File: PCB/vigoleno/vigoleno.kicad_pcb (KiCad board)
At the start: 6 copper layers, 80.8 x 50 mm, 181 parts, among them J1 9P-MSD-PP-V2, J3 USB_OTG, J4 IPEX RF Coaxial Connector SMD, M1 MODULE_RTL8188, U1 MT29F8G08ABABA, U2 ISL8022, U3 ALLWINNER-A13(176-LQFP), U4 TLV62569-SOT23-6, U5 TPS62233DRYR, U6 AS4C256M16D3A-12BAN(96-FBGA), U7 MCP130T-300ITT, Y1 Crystal_GND24_24MHz

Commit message: update March 6 2019
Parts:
- C31, C32, Y1: moved to B.Cu
- moved DEBUG1 49.6 mm to (589.9, -415.9), turned to 180 degrees
- moved D3 24.8 mm to (582.5, -418.7), turned to 0 degrees
- moved J4 24.7 mm to (556.2, -446.9)
- moved D2 19.0 mm to (582.5, -421.9), turned to 0 degrees
- moved JP2 15.2 mm to (558.4, -457.5), turned to 270 degrees
- moved C97 12.6 mm to (560.9, -456.8), turned to 180 degrees
- moved L6 11.8 mm to (558.4, -454.4), turned to 270 degrees
- moved C98 10.7 mm to (561.4, -455.6), turned to 180 degrees
- moved C31 10.5 mm to (613.0, -432.0), turned to 0 degrees
- moved C32 7.32 mm to (615.4, -432.0), turned to 180 degrees
- moved Y1 5.92 mm to (614.1, -434.3), turned to 0 degrees
- moved R18 2.88 mm to (592.1, -422.2), turned to 90 degrees
- moved R17 2.86 mm to (584.2, -454.1)
- moved LED1 2.56 mm to (584.3, -455.4)
- moved C67 1.57 mm to (593.1, -422.2), turned to 270 degrees
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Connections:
- GPIO1 pad 10: /PIN39_USBH-EN -> /TWI2-SCK
- GPIO1 pad 11: /PIN38_VGA-DIS -> /USB0-IDDET
- GPIO1 pad 12: /PIN37_LED1 -> /TWI2-SDA
- GPIO1 pad 13: /PIN15_NCE1 -> /SPI2-MOSI
- GPIO1 pad 14: /USB0-DRV -> /SPI2-CS0
- GPIO1 pad 15: /USB0-VBUSDET -> /SPI2-MISO
- GPIO1 pad 16: /USB0-IDDET -> /SPI2-CLK
- GPIO1 pad 21: /PIN36 -> /LCD-VSYNC
- GPIO1 pad 22: /PIN35 -> /USB0-VBUSDET
- GPIO1 pad 23: /PIN34 -> /LCD-HSYNC
- GPIO1 pad 24: /PIN33 -> /USB0-DRV
- GPIO1 pad 25: /PIN32 -> /LCD-DE
- GPIO1 pad 26: /PIN31 -> /PIN39_USBH-EN
- GPIO1 pad 27: /PIN28_NDQS -> /LCD-CLK
- GPIO1 pad 28: /PIN19_NRB1 -> /PIN38_VGA-DIS
- GPIO1 pad 29: /PIN30 -> /LCD-D23
- GPIO1 pad 30: /PIN29 -> /PIN37_LED1
- GPIO1 pad 31: /SPI2-MISO -> /LCD-D22
- GPIO1 pad 32: /SPI2-MOSI -> /PIN36
- GPIO1 pad 33: /SPI2-CLK -> /LCD-D21
- GPIO1 pad 34: /SPI2-CS0 -> /PIN35
- GPIO1 pad 35: /PIN11_TWI1-SDA -> /LCD-D20
- GPIO1 pad 36: /TWI2-SCK -> /PIN34
- GPIO1 pad 37: /PIN10_TWI1-SCK -> /LCD-D19
- GPIO1 pad 38: /TWI2-SDA -> /PIN33
- GPIO1 pad 39: /PIN8 -> /LCD-D18
- GPIO1 pad 40: /PIN9 -> /PIN32
- GPIO1 pad 41: /PIN6_PWM0 -> /LCD-D15
- GPIO1 pad 42: /PIN7 -> /PIN31
- GPIO1 pad 43: /LCD-D23 -> /LCD-D14
- GPIO1 pad 44: /LCD-D22 -> /PIN30
- GPIO1 pad 45: /LCD-D21 -> /LCD-D13
- GPIO1 pad 46: /LCD-D20 -> /PIN29
- GPIO1 pad 47: /LCD-D19 -> /LCD-D12
- GPIO1 pad 48: /LCD-D18 -> /PIN28_NDQS
- GPIO1 pad 49: /LCD-D15 -> /LCD-D11
- GPIO1 pad 50: /LCD-D14 -> /PIN19_NRB1
- GPIO1 pad 51: /LCD-D13 -> /LCD-D10
- GPIO1 pad 52: /LCD-D12 -> /PIN15_NCE1
- GPIO1 pad 53: /LCD-D11 -> /LCD-D7
- GPIO1 pad 54: /LCD-D10 -> /PIN11_TWI1-SDA
- GPIO1 pad 56: /LCD-D7 -> /PIN10_TWI1-SCK
- GPIO1 pad 57: /LCD-D4 -> /LCD-D5
- GPIO1 pad 58: /LCD-D5 -> /PIN9
- GPIO1 pad 59: /LCD-D2 -> /LCD-D4
- GPIO1 pad 60: /LCD-D3 -> /PIN8
- GPIO1 pad 61: /LCD-HSYNC -> /LCD-D3
- GPIO1 pad 62: /LCD-VSYNC -> /PIN7
- GPIO1 pad 63: /LCD-CLK -> /LCD-D2
- GPIO1 pad 64: /LCD-DE -> /PIN6_PWM0
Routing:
- net /TPX2: track 59.8 -> 9.97 mm, vias 3 -> 1
- net /LCD-D19: track 1.81 -> 50.7 mm, vias 0 -> 2
- net /TPY2: track 58.3 -> 9.81 mm, vias 3 -> 1
- net /LCD-D10: track 2.32 -> 49.0 mm, vias 0 -> 2
- net /LCD-D15: track 1.77 -> 48.4 mm, vias 0 -> 2
- net /LCD-D20: track 1.81 -> 47.6 mm, vias 0 -> 2
- net /LCD-D18: track 1.86 -> 45.9 mm, vias 0 -> 2
- net /LCD-D13: track 1.80 -> 45.7 mm, vias 0 -> 2
- net /LCD-D14: track 1.84 -> 45.5 mm, vias 0 -> 2
- net /LCD-D4: track 1.87 -> 44.0 mm, vias 0 -> 2
- net /LCD-D11: track 1.86 -> 43.7 mm, vias 0 -> 2
- net /LCD-D12: track 1.85 -> 43.5 mm, vias 0 -> 2
- net /LCD-D5: track 1.45 -> 40.5 mm, vias 0 -> 2
- net /LCD-D2: track 1.45 -> 40.0 mm, vias 0 -> 2
- net /LCD-D3: track 1.72 -> 39.8 mm, vias 0 -> 2
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
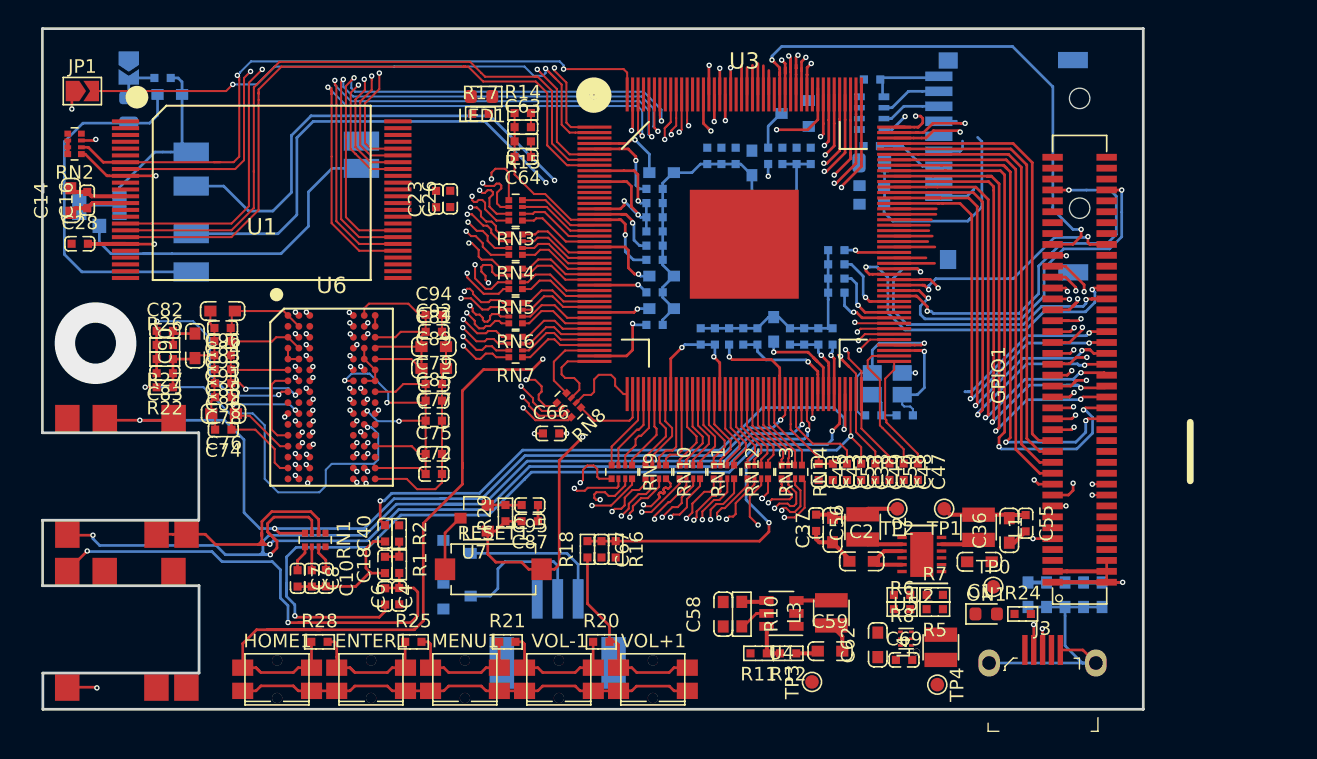
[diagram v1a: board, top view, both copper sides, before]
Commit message: finished VIGOLENO SBC PCB layout
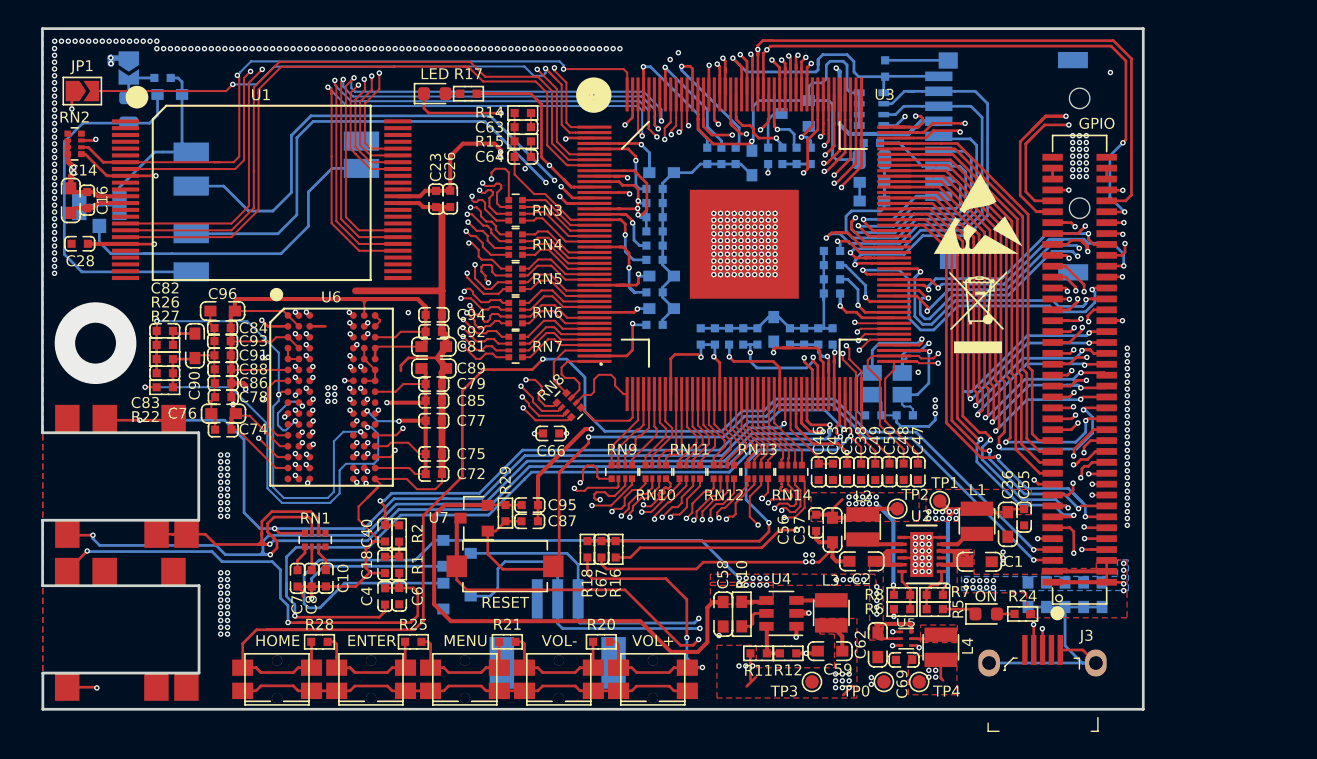
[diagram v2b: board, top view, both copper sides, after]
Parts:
- added G***: LOGO, MyKiCadLib:dfm18x13_logo, F.Cu at (584.5, -432.8)
- added REF**: ESD-Logo_6.6x6mm_SilkScreen, Symbol:ESD-Logo_6.6x6mm_SilkScreen, F.Cu at (620.8, -446.8)
- added REF**: WEEE-Logo_4.2x6mm_SilkScreen, Symbol:WEEE-Logo_4.2x6mm_SilkScreen, F.Cu at (620.8, -439.6)
- moved TP0 10.6 mm to (613.8, -412.4)
- moved LED 3.44 mm to (580.9, -455.6), turned to 0 degrees
- moved R17 1.72 mm to (583.3, -455.6)
- moved TP4 1.34 mm to (616.4, -412.4)
- moved R23 1.25 mm to (613.9, -457.5), turned to 270 degrees
- moved RESET 0.89 mm to (586.0, -420.9)
- moved TP1 0.66 mm to (617.9, -425.7)
- moved C36 0.45 mm to (622.9, -424.0)
- moved C55 0.45 mm to (624.1, -424.5)
- moved L1 0.45 mm to (620.7, -424.2)
- moved C15 0.33 mm to (610.0, -443.0)
- moved C22 0.33 mm to (610.0, -440.9)
- moved C27 0.33 mm to (610.0, -444.1)
- moved C30 0.33 mm to (610.0, -442.0)
- moved RN15 0.29 mm to (612.9, -454.5)
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- renumbered DEBUG1 to DEBUG, ENTER1 to ENTER, GPIO1 to GPIO, H-P1 to H-P, HOME1 to HOME, LED1 to LED, MENU1 to MENU, MIC1 to MIC, ON1 to ON, RESET1 to RESET, VOL+1 to VOL+, VOL-1 to VOL-
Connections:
- C72 pad 1: Net-(C72-Pad1) -> /+1.5V
- C74 pad 1: Net-(C72-Pad1) -> /+1.5V
- C75 pad 1: Net-(C72-Pad1) -> /+1.5V
- C76 pad 1: Net-(C72-Pad1) -> /+1.5V
- C77 pad 1: Net-(C72-Pad1) -> /+1.5V
- C78 pad 1: Net-(C72-Pad1) -> /+1.5V
- C79 pad 1: Net-(C72-Pad1) -> /+1.5V
- C81 pad 1: Net-(C72-Pad1) -> /+1.5V
- C84 pad 1: Net-(C72-Pad1) -> /+1.5V
- C85 pad 1: Net-(C72-Pad1) -> /+1.5V
- C86 pad 1: Net-(C72-Pad1) -> /+1.5V
- C88 pad 1: Net-(C72-Pad1) -> /+1.5V
- C89 pad 1: Net-(C72-Pad1) -> /+1.5V
- C91 pad 1: Net-(C72-Pad1) -> /+1.5V
- C92 pad 1: Net-(C72-Pad1) -> /+1.5V
- C93 pad 1: Net-(C72-Pad1) -> /+1.5V
- C94 pad 1: Net-(C72-Pad1) -> /+1.5V
- C96 pad 1: Net-(C72-Pad1) -> /+1.5V
- U6 pad A1: Net-(C72-Pad1) -> /+1.5V
- U6 pad A8: Net-(C72-Pad1) -> /+1.5V
- U6 pad B2: Net-(C72-Pad1) -> /+1.5V
- U6 pad C1: Net-(C72-Pad1) -> /+1.5V
- U6 pad C9: Net-(C72-Pad1) -> /+1.5V
- U6 pad D2: Net-(C72-Pad1) -> /+1.5V
- U6 pad D9: Net-(C72-Pad1) -> /+1.5V
- U6 pad E9: Net-(C72-Pad1) -> /+1.5V
- U6 pad F1: Net-(C72-Pad1) -> /+1.5V
- U6 pad G7: Net-(C72-Pad1) -> /+1.5V
- U6 pad H2: Net-(C72-Pad1) -> /+1.5V
- U6 pad H9: Net-(C72-Pad1) -> /+1.5V
- U6 pad K2: Net-(C72-Pad1) -> /+1.5V
- U6 pad K8: Net-(C72-Pad1) -> /+1.5V
- U6 pad N1: Net-(C72-Pad1) -> /+1.5V
- U6 pad N9: Net-(C72-Pad1) -> /+1.5V
- U6 pad R1: Net-(C72-Pad1) -> /+1.5V
- U6 pad R9: Net-(C72-Pad1) -> /+1.5V
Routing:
- net +3V3: track 56.4 -> 403.1 mm, vias 4 -> 48
- net /+1.5V: track 28.1 -> 296.9 mm, vias 5 -> 25
- net /+1.2V-CPU: track 30.8 -> 203.7 mm, vias 4 -> 19
- net GND: track 200.9 -> 348.4 mm, vias 6 -> 371
- net /UART1-TX: track 13.1 -> 126.1 mm, vias 0 -> 3
- net /UART1-RX: track 12.9 -> 124.0 mm, vias 0 -> 5
- net Net-(C72-Pad1): track 98.8 -> 0.00 mm, vias 8 -> 0
- net /+1.2V-INT: track 26.6 -> 117.8 mm, vias 4 -> 16
- net /PIN19_NRB1: track 2.68 -> 80.6 mm, vias 1 -> 2
- net /PIN37_LED1: track 0.00 -> 74.1 mm, vias 0 -> 2
- net /NMI-N: track 8.22 -> 80.6 mm, vias 2 -> 3
- net /USB0-IDDET: track 2.14 -> 72.7 mm, vias 0 -> 2
- net /+3.0VA: track 7.22 -> 77.6 mm, vias 1 -> 7
- net /PIN15_NCE1: track 0.00 -> 69.2 mm, vias 0 -> 2
- net /PIN9: track 0.00 -> 65.5 mm, vias 0 -> 2
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- added copper zone on B.Cu, net +3V3
- added copper zone on F.Cu, net +3V3
- added copper zone on L3.Cu, net +3V3
- added copper zone on F.Cu, net /+1.2V-CPU
- added copper zone on L3.Cu, net /+1.2V-CPU
- added copper zone on F.Cu, net /+1.2V-INT
- added copper zone on L3.Cu, net /+1.2V-INT
- added copper zone on F.Cu, net /+1.5V
- added copper zone on L3.Cu, net /+1.5V
- added copper zone on F.Cu, net /+3.0VA
- added copper zone on L3.Cu, net /+3.0VA
- added copper zone on B.Cu, net GND
- added copper zone on F.Cu, net GND
- added copper zone on L1.Cu, net GND
- added copper zone on L2.Cu, net GND
- added copper zone on L3.Cu, net GND
- added copper zone on L4.Cu, net GND
- added copper zone on F.Cu, net Net-(L4-Pad1)
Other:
- board text added: "Designed by Tran Thien Nhan"
- board text added: "GND"
- board text added: "RX"
- board text added: "TX"
- board text added: "VIGOLENO"
